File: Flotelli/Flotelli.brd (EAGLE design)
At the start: 120.3 x 60 mm, 64 parts, among them J1 FTDI-SER-6-PP, J3 DF12-32-DP, J4 DF12-60-DP, U3 STM32F429-LQFP144, Y1-C1 22pF, Y1-C2 22pF, Y1-R1 390R

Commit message: Update Flotelli
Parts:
- C1, C10, C11, C12, C13, C14, C15, C16, C17, C18, C2, C3, C4, C5, C6, C7, C8, C9, Y1-C1, Y1-C2: device ell-i:0402 -> ELL-i-Passives:C0402
- D2: device ell-i:DIODE0603 -> SparkFun-LED:LED-0603
- J3: value DF12-32-DP -> DF12-32DP-0.5V; device ell-i:DF12-32-DP -> ELL-i-Connectors:DF12(4.0)-32DP-0.5V
- J4: value DF12-60-DP -> DF12-60DP; device ell-i:DF12-60-DP -> ELL-i-Connectors:DF12(4.0)-60DP-0.5V
- R1, R2, R33, Y1-R1: device ell-i:0402 -> ELL-i-Passives:R0402
- SV2, SV3, SV4, SV5: value (none) -> M09LOCK; device con-lstb:MA09-1 -> SparkFun-Connectors:1X09_LOCK
- U1: device ell-i:QFN24_4MM-H -> ELL-i-DigitalIC:QFN-24_4MM-H
- U3: value STM32F429-LQFP144 -> STM32F429ZIT; device ell-i:LQFP144 -> ELL-i-DigitalIC:LQFP144
- moved SV2 10.2 mm to (25.4, 6.35), flipped to the bottom
- moved SV4 10.2 mm to (25.4, 47.0), flipped to the bottom
- moved SV3 10.2 mm to (48.3, 6.35), flipped to the bottom
- moved SV5 10.2 mm to (48.3, 47.0), flipped to the bottom
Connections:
- net +3V3: now also D2.A; no longer D2.2
- net N41567: now also D2.C; no longer D2.1
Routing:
- net +3V3: track 59.2 -> 60.3 mm

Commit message: Replaced FTDI header with a new one
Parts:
- J1: device ell-i:FTDI-SER-6-SIL -> ELL-i-Connectors:FTDI-SER-6-SIL
- turned J1 to 0 degrees
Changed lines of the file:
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@@
 <layer number="220" name="220bmp" color="7" fill="1" visible="no" active="yes"/>
 <layer number="221" name="connection" color="7" fill="1" visible="no" active="yes"/>
+<layer number="222" name="222bmp" color="7" fill="1" visible="yes" active="yes"/>
 <layer number="223" name="223bmp" color="7" fill="1" visible="no" active="yes"/>
 <layer number="224" name="224bmp" color="7" fill="1" visible="no" active="yes"/>
@@
 <element name="R1" library="ELL-i-Passives" package="R0402" value="150R" x="30" y="50.5" rot="R180"/>
 <element name="R33" library="ELL-i-Passives" package="R0402" value="1k5" x="14.08" y="37.27" rot="R270"/>
-<element name="J1" library="ell-i" package="FTDI-SER-6-SIL" value="FTDI-SER-6-PP" x="18.39" y="50.62" rot="R90"/>
+<element name="J1" library="ELL-i-Connectors" package="FTDI-SER-6-SIL" value="FTDI-SER-6-PP" x="18.39" y="50.62"/>
 <element name="PC14" library="testpad" package="B1,27" value="TPSB1,27" x="8.31" y="10.31">
 <attribute name="TP_SIGNAL_NAME" value="" x="8.31" y="14.31" size="1.778" layer="27" display="off"/>

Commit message: Replaces the 6-pin female header on Flotelli
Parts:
- SV6: device con-lsta:FE06W -> ELL-i-Connectors:1X06-THT-FEMALE-ANGLE90
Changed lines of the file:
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@@
 <?xml version="1.0" encoding="utf-8"?>
 <!DOCTYPE eagle SYSTEM "eagle.dtd">
-<eagle version="6.4">
+<eagle version="6.5.0">
 <drawing>
 <settings>
@@
 <layer number="220" name="220bmp" color="7" fill="1" visible="no" active="yes"/>
 <layer number="221" name="connection" color="7" fill="1" visible="no" active="yes"/>
-<layer number="222" name="222bmp" color="7" fill="1" visible="yes" active="yes"/>
 <layer number="223" name="223bmp" color="7" fill="1" visible="no" active="yes"/>
 <layer number="224" name="224bmp" color="7" fill="1" visible="no" active="yes"/>
@@
 <element name="SV4" library="SparkFun-Connectors" package="1X09_LOCK" value="M09LOCK" x="25.4" y="46.99" rot="MR0"/>
 <element name="SV5" library="SparkFun-Connectors" package="1X09_LOCK" value="M09LOCK" x="48.26" y="46.99" rot="MR0"/>
-<element name="SV6" library="con-lsta" package="FE06W" value="" x="41.91" y="22.86" rot="R270">
-<attribute name="OC_NEWARK" value="unknown" x="41.91" y="22.86" size="1.778" layer="27" rot="R270" display="off"/>
-<attribute name="MPN" value="" x="41.91" y="22.86" size="1.778" layer="27" rot="R270" display="off"/>
-<attribute name="MF" value="" x="41.91" y="22.86" size="1.778" layer="27" rot="R270" display="off"/>
-<attribute name="OC_FARNELL" value="unknown" x="41.91" y="22.86" size="1.778" layer="27" rot="R270" display="off"/>
-</element>
+<element name="SV6" library="ELL-i-Connectors" package="1X06-THT-FEMALE-ANGLE90" value="" x="41.91" y="22.86" rot="R270"/>
 <element name="C10" library="ELL-i-Passives" package="C0402" value="100nF" x="6.31" y="25.81" rot="R270"/>
 <element name="C11" library="ELL-i-Passives" package="C0402" value="100nF" x="6.31" y="20.81" rot="R270"/>

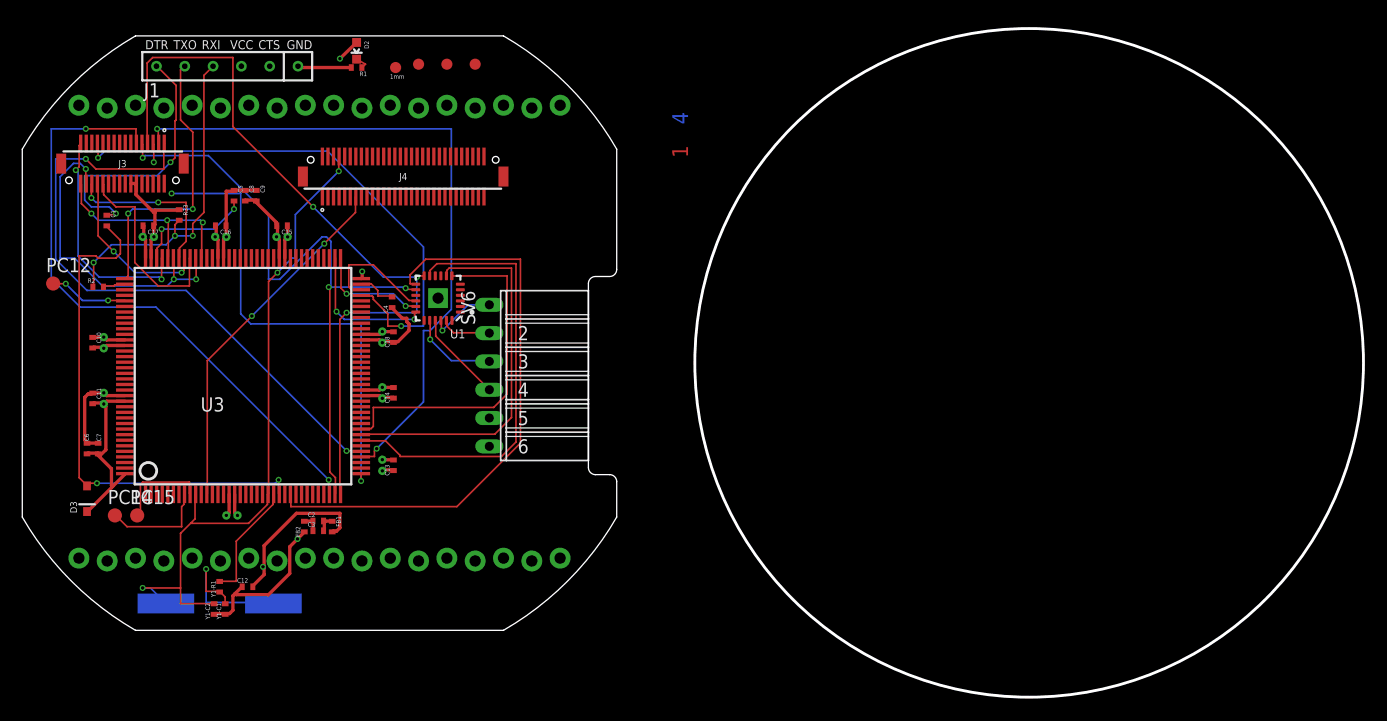
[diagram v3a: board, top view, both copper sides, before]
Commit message: Flotelli pins defined per the latest pin order table.
There are still some errors in the table.  We will fix them next.

Also has Flotelli brd, very preliminary.
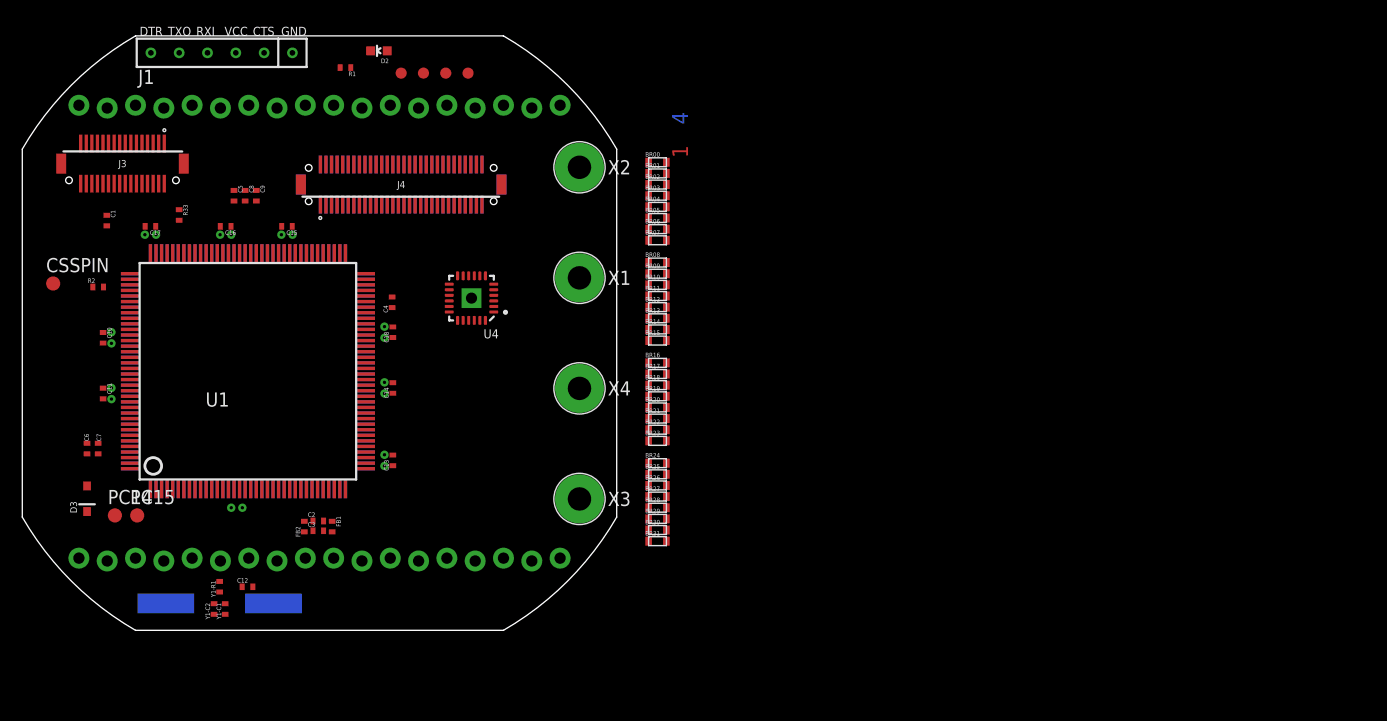
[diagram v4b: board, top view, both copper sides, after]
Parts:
- removed SV6: (no value), ELL-i-Connectors:1X06-THT-FEMALE-ANGLE90
- removed U3: STM32F429ZIT, ELL-i-DigitalIC:LQFP144
- added BR00, BR01, BR02, BR03, BR04, BR05, BR06, BR07, BR08, BR09, BR10, BR11, BR12, BR13, BR14, BR15, BR16, BR17, BR18, BR19, BR20, BR21, BR22, BR23, BR24, BR25, BR26, BR27, BR28, BR29, BR30, BR31: 100, ELL-i-Passives:R0603
- added J2: DF12-ELLI-RECEPTABLE-BOTTOM, ELL-i-Connectors:DF12-60DS-0.5V
- added U2: LCMXO2-2000HC-4TG144, ELL-i-DigitalIC:TQFP144
- added U4: (no value), ELL-i-DigitalIC:QFN-24_4MM-H
- added X1, X2, X3, X4: M-BOLT-2, ELL-i-Connectors:M2-1
- FID1: value FIDUCIAL1X2.5 -> FIDUCIAL""; device microbuilder:FIDUCIAL-1X2.5 -> microbuilder:FIDUCIAL_1MM
- J4: value DF12-60DP -> DF12-ELLI-HEADER-TOP
- U1: value (none) -> STM32F429ZIT; device ELL-i-DigitalIC:QFN-24_4MM-H -> ELL-i-DigitalIC:LQFP144
- moved U1 18.3 mm to (20.2, 23.2), turned to 0 degrees
- moved D2 2.00 mm to (32.0, 52.0), turned to 90 degrees
- moved J1 1.30 mm to (17.9, 51.8)
- moved C10 1.04 mm to (7.25, 26.2)
- moved C11 1.04 mm to (7.25, 21.2)
- moved FID4 1.02 mm to (40.0, 50.0)
- moved R1 1.00 mm to (29.0, 50.5)
- moved FID2 0.91 mm to (36.0, 50.0)
- moved VIA1 0.82 mm to (8.00, 20.8)
- moved VIA17 0.82 mm to (8.00, 25.8)
- moved VIA18 0.82 mm to (8.00, 26.8)
- moved VIA6 0.82 mm to (8.00, 21.8)
- moved VIA13 0.82 mm to (19.8, 11.0)
- moved VIA14 0.82 mm to (18.8, 11.0)
- moved FID3 0.81 mm to (38.0, 50.0)
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- renumbered PC12 to CSSPIN
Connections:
- removed net AD0: J3.11, U3.34
- removed net AD1-ETH_REF_CLK: J3.9, U1.14, U3.35
- removed net AD10: U3.26
- removed net AD11-ETH_MDC: U1.13, U3.27
- removed net AD12: U3.28
- removed net AD13: U3.29
- removed net AD14-ETH_RXD0: U1.8, U3.44
- removed net AD15-ETH_RXD1: U1.7, U3.45
- removed net AD2-ETH_MDIO: J3.7, U1.12, U3.36
- removed net AD3: J3.5, U3.37
- removed net AD4: J3.3, U3.40
- removed net AD5: J3.1, U3.41
- removed net AD6: U3.42
- removed net AD7-ETH_CRSDV: U1.11, U3.43
- removed net AD8: U3.46
- removed net AD9: U3.47
- removed net ETH_TEX_EN: U1.16, U3.70
- removed net IO0: J3.24, U3.100
- removed net IO1: J3.26, U3.101
- removed net IO2: J3.28, U3.102
- removed net IO3: J3.30, U3.103, U3.99
- removed net IO4: J3.32, U3.104, U3.98
- removed net IO5: J3.31, U3.105
- removed net IO8: J3.25, U3.69
- removed net MISO1: U3.134
- removed net MISO_ETH: U3.75
- removed net MOSI1: U3.135
- removed net MOSI_ETH: U3.76
- removed net N$1: U3.48
- removed net N$9: CSSPIN.TP, U3.113
- removed net PB6: U3.136
- removed net PB7: U3.137
- removed net PD2: U3.116
- removed net PF2: J4.13, U3.12
- removed net RX2: R2.2, U3.110
- removed net SCK1: U3.133
- removed net SCL1: U3.139
- removed net SDA1: U3.140
- removed net SPR1: U3.96
- removed net SPR2: U3.97
- removed net TX2: J1.RXD, U3.109
- new net 3.3V: J2.6, J4.6
- new net 5V: J2.8, J4.8
- new net A0: J3.11, U1.34
- new net A1: U1.18
- new net A2: J3.3, U1.40
- new net A3: J3.1, U1.41
- new net A4: U1.140
- new net A5: U1.136
- new net CSSPIN: CSSPIN.TP, U1.113
- new net D0: J3.28, U1.102
- new net D1: J3.26, U1.101
- new net D10: R2.2, U1.110
- new net D11: U1.135
- new net D12: U1.42
- new net D13: U1.133
- new net D2: U1.116
- new net D5: U1.47
- new net D6: J3.5, U1.37
- new net D7: U1.139
- new net D8: U1.91
- new net D9: U1.46
- new net E0: U1.19
- new net E1: U1.20
- new net E10: U1.96
- new net E11: U1.97
- new net E12: U1.70
- new net E13: J3.25, U1.69
- new net E14: U1.73
- new net E15: U1.76
- new net E16: U1.75
- new net E17: U1.74
- new net E18: U1.112
- new net E19: U1.111
- new net E2: U1.21
- new net E3: U1.22
- new net E8: U1.92
- new net ETH_CLK: J3.9, U1.35, U4.14
- new net ETH_CRS: U1.43, U4.11
- new net ETH_MDC: U1.27, U4.13
- new net ETH_MDIO: J3.7, U1.36, U4.12
- new net ETH_RXD0: U1.44, U4.8
- new net ETH_RXD1: U1.45, U4.7
- new net ETH_TXEN: U1.126, U4.16
- new net FPGA_SN: U1.48
- new net GND: J2.12, J2.14, J4.12, J4.14
- new net JTCK: J1.RXD, U1.109
- new net JTDI: J3.30, U1.103, U1.99
- new net JTMS: J3.31, U1.105
- new net JTRST: U1.134
- new net MCO: J3.24, U1.100
- new net MEM_A0: U1.10
- new net MEM_A1: U1.11
- new net MEM_A10: U1.56, U1.57
- new net MEM_A12: U1.87
- new net MEM_A13: U1.88
- new net MEM_A14: U1.89
- new net MEM_A15: U1.90
- new net MEM_A16: U1.80, U2.21
- new net MEM_A17: U1.81, U2.22
- new net MEM_A18: U1.82, U2.23
- new net MEM_A19: U1.2, U2.24
- new net MEM_A2: U1.12
- new net MEM_A20: U1.3
- new net MEM_A21: U1.4, U2.42
- new net MEM_A22: U1.5, U2.61
- new net MEM_A23: U1.1, U2.62
- new net MEM_A3: U1.13
- new net MEM_A4: U1.14
- new net MEM_A5: U1.15
- new net MEM_A6: U1.50
- new net MEM_A7: U1.53
- new net MEM_A8: U1.54
- new net MEM_A9: U1.55
- new net MEM_CLK: U1.117
- new net MEM_CS1: U1.123, U2.50
- new net MEM_CS2: U1.124
- new net MEM_CS3: U1.125
- new net MEM_CS4: U1.127
- new net MEM_D0: U1.85, U2.1
- new net MEM_D1: U1.86, U2.2
- new net MEM_D10: U1.66, U2.13
- new net MEM_D11: U1.67, U2.14
- new net MEM_D12: U1.68, U2.15
- new net MEM_D13: U1.77, U2.17
- new net MEM_D14: U1.78, U2.19
- new net MEM_D15: U1.79, U2.20
- new net MEM_D2: U1.114, U2.3
- new net MEM_D3: U1.115, U2.4
- new net MEM_D4: U1.58, U2.5
- new net MEM_D5: U1.59, U2.6
- new net MEM_D6: U1.60, U2.9
- new net MEM_D7: U1.63, U2.10
- new net MEM_D8: U1.64, U2.11
- new net MEM_D9: U1.65, U2.12
- new net MEM_NADV: U1.137
- new net MEM_NBL0: U1.141
- new net MEM_NBL1: U1.142
- new net MEM_NOE: U1.118
- new net MEM_NWAIT: U1.122
- new net MEM_NWE: U1.119
- new net MEM_SDCKE0: U1.29
- new net MEM_SDCLK: U1.93
- new net MEM_SDNCAS: U1.132
- new net MEM_SDNE0: U1.28
- new net MEM_SDNRAS: U1.49
- new net MEM_SDWNE: U1.26
- new net PROGRAMN: J3.32, U1.104, U1.98
- new net VCC(IO): J2.2, J4.2
- net +3V3: now also U1.108, U1.121, U1.131, U1.144, U1.17, U1.30, U1.39, U1.52, U1.6, U1.62, U1.72, U1.84, U1.95; no longer U3.108, U3.121, U3.131, U3.144, U3.17, U3.30, U3.39, U3.52, U3.6, U3.62, U3.72, U3.84, U3.95
- net BOOT0: now also U1.138; no longer U3.138
- net ETH_NRST: now also U4.15; no longer U1.15
- net ETH_RXER: now also U4.10; no longer U1.10
- net ETH_TXD0: now also U1.128, U4.17; no longer U1.17, U3.73
- net ETH_TXD1: now also U1.129, U4.18; no longer U1.18, U3.74
- net GNDI: now also U1.107, U1.120, U1.130, U1.16, U1.38, U1.51, U1.61, U1.83, U1.94, U4.THERM, X2.1; no longer SV6.5, U1.THERM, U3.107, U3.120, U3.130, U3.16, U3.38, U3.51, U3.61, U3.83, U3.94
- net N$10: now also U4.21; no longer SV6.4, U1.21
- net N$11: now also U4.20; no longer SV6.3, U1.20
- net N$2: now also U1.8; no longer U3.8
- net N$3: now also U1.9; no longer U3.9
- net N$4: now also U1.71; no longer U3.71
- net N$5: now also U1.106; no longer U3.106
- net N$7: now also U4.22; no longer SV6.1, U1.22
- net N$8: now also U4.23; no longer SV6.2, U1.23
- net N100630: now also U1.33; no longer U3.33
- net N98218: now also U1.31; no longer U3.31
- net NRES: now also U1.25; no longer U3.25
- net PF0: now also U1.23; no longer J4.8, U3.10, U3.23
- net PF1: now also U1.24; no longer U3.24
- net RTC: now also U1.7; no longer U3.7
- net V-POE: now also X1.1; no longer SV6.6
- net VBATT: now also J2.4, J4.4
- net VIN: now also J2.10, J4.10
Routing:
- net AD2-ETH_MDIO: track 70.3 -> 0.00 mm, vias 3 -> 0
- net GNDI: track 67.8 -> 0.00 mm, vias 1 -> 0
- net AD4: track 61.6 -> 0.00 mm, vias 2 -> 0
- net PF0: track 61.1 -> 0.00 mm, vias 3 -> 0
- net +3V3: track 60.3 -> 0.00 mm, vias 3 -> 0
- net AD1-ETH_REF_CLK: track 58.9 -> 0.00 mm, vias 3 -> 0
- net AD0: track 56.1 -> 0.00 mm, vias 2 -> 0
- net AD5: track 55.9 -> 0.00 mm, vias 2 -> 0
- net AD11-ETH_MDC: track 52.4 -> 0.00 mm
- net IO8: track 48.9 -> 0.00 mm, vias 2 -> 0
- net AD3: track 48.6 -> 0.00 mm, vias 3 -> 0
- net NRES: track 46.9 -> 0.00 mm, vias 2 -> 0
- net AD7-ETH_CRSDV: track 39.5 -> 0.00 mm
- net AD14-ETH_RXD0: track 33.9 -> 0.00 mm
- net PF2: track 32.2 -> 0.00 mm, vias 2 -> 0
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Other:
- board size 120.3 x 60 mm -> 53.3 x 53.3 mm
